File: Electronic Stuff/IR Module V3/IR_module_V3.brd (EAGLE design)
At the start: 45.4 x 43.2 mm, 20 parts, among them IC1 74HCT02N, Q1 IRF540, Q2 16M

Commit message: Added texts
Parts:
- C1, C2, C3, C4: device SparkFun-Passives:CAP-PTH-LARGE -> SparkFun-Capacitors:CAP-PTH-SMALLEZ
- moved C4 3.93 mm to (9.84, 25.4)
- moved C3 3.82 mm to (6.03, 22.9), turned to 90 degrees
- moved C1 3.81 mm to (12.7, 6.35)
- moved C2 3.49 mm to (12.4, 21.6)
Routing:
- net 12V: track 49.9 -> 42.1 mm
- net VCC: track 120.5 -> 127.7 mm
- net GND: track 151.2 -> 146.4 mm, vias 3 -> 4
- net RESET: track 13.4 -> 17.7 mm
- net N$8: track 15.3 -> 16.6 mm
- net XTAL1: track 15.6 -> 14.7 mm
- net XTAL2: track 15.6 -> 14.9 mm
- added copper zone on layer 1, net N$1
- added copper zone on layer 16, net N$6
- removed copper zone on layer 16, net N$1
- removed copper zone on layer 1, net N$6
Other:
- board text added: "GaTech VIP - RoboSense"
- board text added: "High PWR"
- board text added: "IR Module"
- board text added: "Low PWR"
- board text added: "RX"
- board text added: "SeaPerch Project"
- board text added: "TX"
- board text added: "Version 0.3"
- board text removed: "100n"
- board text removed: "22p"

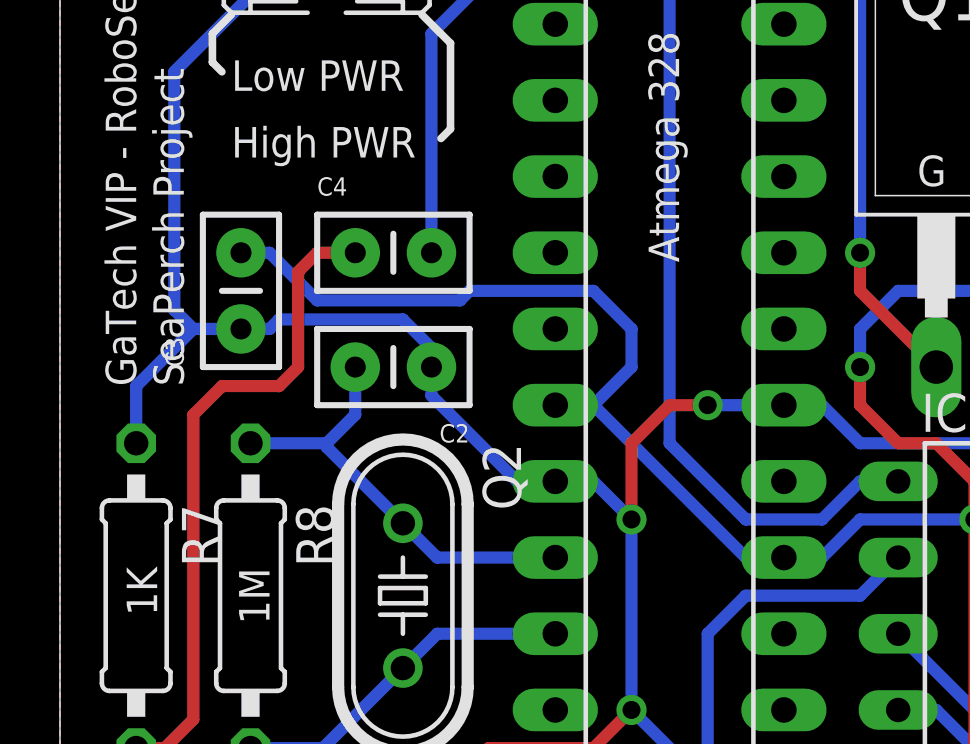
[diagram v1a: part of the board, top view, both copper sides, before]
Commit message: Minor Adjustment for Manufacturing
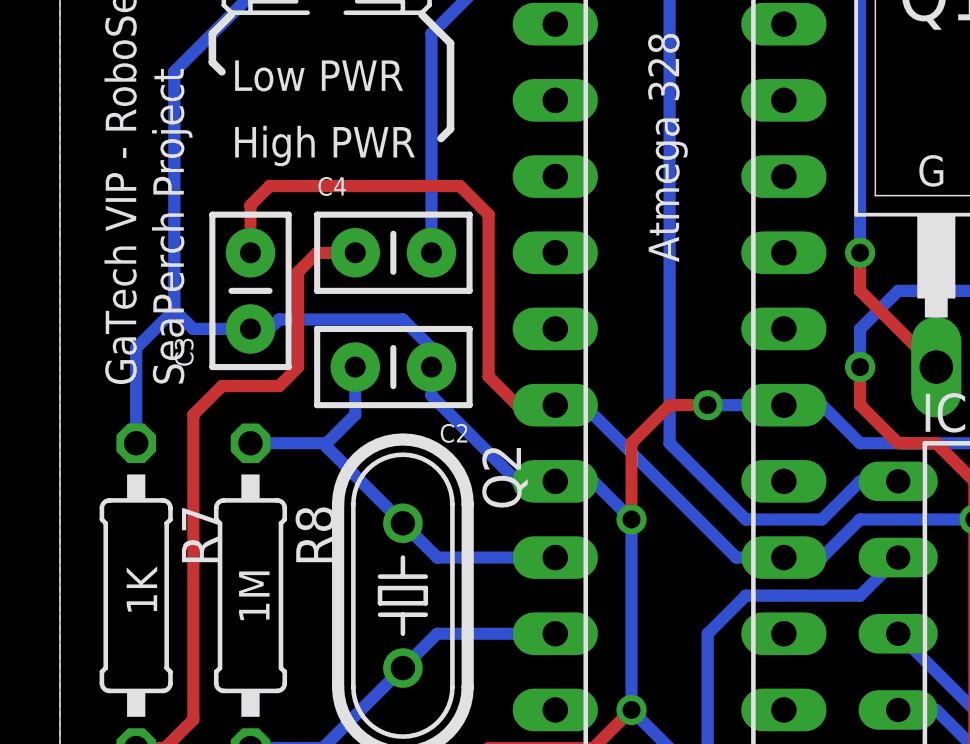
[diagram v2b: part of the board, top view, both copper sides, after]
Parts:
- moved C3 0.32 mm to (6.35, 22.9)
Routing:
- net VCC: track 127.7 -> 128.5 mm
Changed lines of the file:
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@@
 <element name="C1" library="SparkFun-Capacitors" package="CAP-PTH-SMALLEZ" value="22p" x="12.7" y="6.35" rot="R180"/>
 <element name="C2" library="SparkFun-Capacitors" package="CAP-PTH-SMALLEZ" value="22p" x="12.3825" y="21.59" rot="R180"/>
-<element name="C3" library="SparkFun-Capacitors" package="CAP-PTH-SMALLEZ" value="100n" x="6.0325" y="22.86" rot="R90"/>
+<element name="C3" library="SparkFun-Capacitors" package="CAP-PTH-SMALLEZ" value="100n" x="6.35" y="22.86" rot="R90"/>
 <element name="JP3" library="jumper" package="JP2" value="" x="41.91" y="21.59" rot="R270"/>
 <element name="JP7" library="jumper" package="JP1" value="" x="41.91" y="15.24"/>
@@
 <wire x1="3.81" y1="31.4325" x2="3.81" y2="23.495" width="0.4064" layer="16"/>
 <wire x1="3.81" y1="23.495" x2="4.445" y2="22.86" width="0.4064" layer="16"/>
-<wire x1="4.445" y1="22.86" x2="6.0325" y2="22.86" width="0.4064" layer="16"/>
-<wire x1="2.54" y1="19.05" x2="2.54" y2="20.955" width="0.4064" layer="16"/>
-<wire x1="2.54" y1="20.955" x2="4.445" y2="22.86" width="0.4064" layer="16"/>
+<wire x1="4.445" y1="22.86" x2="6.35" y2="22.86" width="0.4064" layer="16"/>
 <wire x1="12.3825" y1="21.59" x2="12.3825" y2="20.6375" width="0.4064" layer="16"/>
 <wire x1="12.3825" y1="20.6375" x2="15.24" y2="17.78" width="0.4064" layer="16"/>
@@
 <wire x1="12.3825" y1="22.225" x2="11.43" y2="23.1775" width="0.4064" layer="16"/>
 <wire x1="11.43" y1="23.1775" x2="7.3025" y2="23.1775" width="0.4064" layer="16"/>
-<wire x1="7.3025" y1="23.1775" x2="6.985" y2="22.86" width="0.4064" layer="16"/>
-<wire x1="6.985" y1="22.86" x2="6.0325" y2="22.86" width="0.4064" layer="16"/>
+<wire x1="6.985" y1="22.86" x2="6.35" y2="22.86" width="0.4064" layer="16"/>
 <via x="19.05" y="10.16" extent="1-16" drill="0.6"/>
 <wire x1="14.2875" y1="8.89" x2="12.7" y2="7.3025" width="0.4064" layer="1"/>
@@
 <wire x1="8.255" y1="4.7625" x2="7.62" y2="4.1275" width="0.4064" layer="16"/>
 <wire x1="7.62" y1="4.1275" x2="7.62" y2="2.54" width="0.4064" layer="16"/>
+<wire x1="7.3025" y1="23.1775" x2="6.985" y2="22.86" width="0.4064" layer="16"/>
+<wire x1="2.54" y1="19.05" x2="2.54" y2="22.225" width="0.4064" layer="16"/>
+<wire x1="2.54" y1="22.225" x2="3.81" y2="23.495" width="0.4064" layer="16"/>
 </signal>
 <signal name="VCC">
@@
 <contactref element="ZU4" pad="20"/>
 <contactref element="C3" pad="2"/>
-<wire x1="13.6525" y1="24.13" x2="17.78" y2="24.13" width="0.4064" layer="16"/>
-<wire x1="17.78" y1="24.13" x2="19.05" y2="22.86" width="0.4064" layer="16"/>
-<wire x1="19.05" y1="22.86" x2="19.05" y2="21.59" width="0.4064" layer="16"/>
-<wire x1="19.05" y1="21.59" x2="17.78" y2="20.32" width="0.4064" layer="16"/>
-<wire x1="16.51" y1="20.32" x2="17.78" y2="20.32" width="0.4064" layer="16"/>
-<wire x1="17.78" y1="20.32" x2="22.86" y2="15.24" width="0.4064" layer="16"/>
-<wire x1="22.86" y1="15.24" x2="24.13" y2="15.24" width="0.4064" layer="16"/>
+<wire x1="22.5425" y1="15.24" x2="24.13" y2="15.24" width="0.4064" layer="16"/>
 <wire x1="24.13" y1="15.24" x2="25.4" y2="15.24" width="0.4064" layer="16"/>
 <wire x1="25.4" y1="15.24" x2="26.67" y2="16.51" width="0.4064" layer="16"/>
 <wire x1="26.67" y1="16.51" x2="30.48" y2="16.51" width="0.4064" layer="16"/>
-<wire x1="13.6525" y1="24.13" x2="13.335" y2="23.8125" width="0.4064" layer="16"/>
-<wire x1="13.335" y1="23.8125" x2="8.5725" y2="23.8125" width="0.4064" layer="16"/>
-<wire x1="8.5725" y1="23.8125" x2="6.985" y2="25.4" width="0.4064" layer="16"/>
-<wire x1="6.985" y1="25.4" x2="6.0325" y2="25.4" width="0.4064" layer="16"/>
+<wire x1="22.5425" y1="15.24" x2="17.4625" y2="20.32" width="0.4064" layer="16"/>
+<wire x1="17.4625" y1="20.32" x2="16.51" y2="20.32" width="0.4064" layer="16"/>
+<wire x1="16.51" y1="20.32" x2="15.24" y2="20.32" width="0.4064" layer="1"/>
+<wire x1="15.24" y1="20.32" x2="14.2875" y2="21.2725" width="0.4064" layer="1"/>
+<wire x1="14.2875" y1="21.2725" x2="14.2875" y2="26.67" width="0.4064" layer="1"/>
+<wire x1="14.2875" y1="26.67" x2="13.335" y2="27.6225" width="0.4064" layer="1"/>
+<wire x1="13.335" y1="27.6225" x2="6.985" y2="27.6225" width="0.4064" layer="1"/>
+<wire x1="6.985" y1="27.6225" x2="6.35" y2="26.9875" width="0.4064" layer="1"/>
+<wire x1="6.35" y1="26.9875" x2="6.35" y2="25.4" width="0.4064" layer="1"/>
 </signal>
 <signal name="RESET">
